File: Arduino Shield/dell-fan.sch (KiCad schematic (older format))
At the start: 49 parts, among them J1 Power, P1 Digital, P10 CONN_01X01, P11 CONN_01X01, P13 CONN_01X01, P2 Power, P3 Analog, P4 Analog, P5 PWM, P6 PWM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

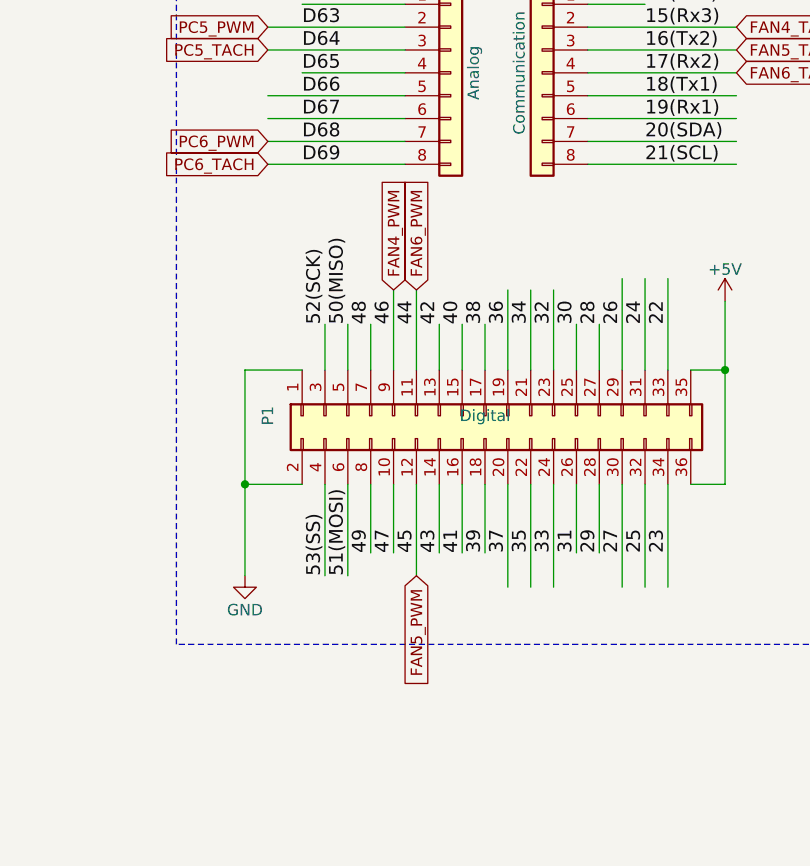
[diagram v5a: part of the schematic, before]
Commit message: redesign for rev 2.01.  Swapped PC and FAN location, and swapped FAN4_PWM and FAN5_PWM pins for simplicity
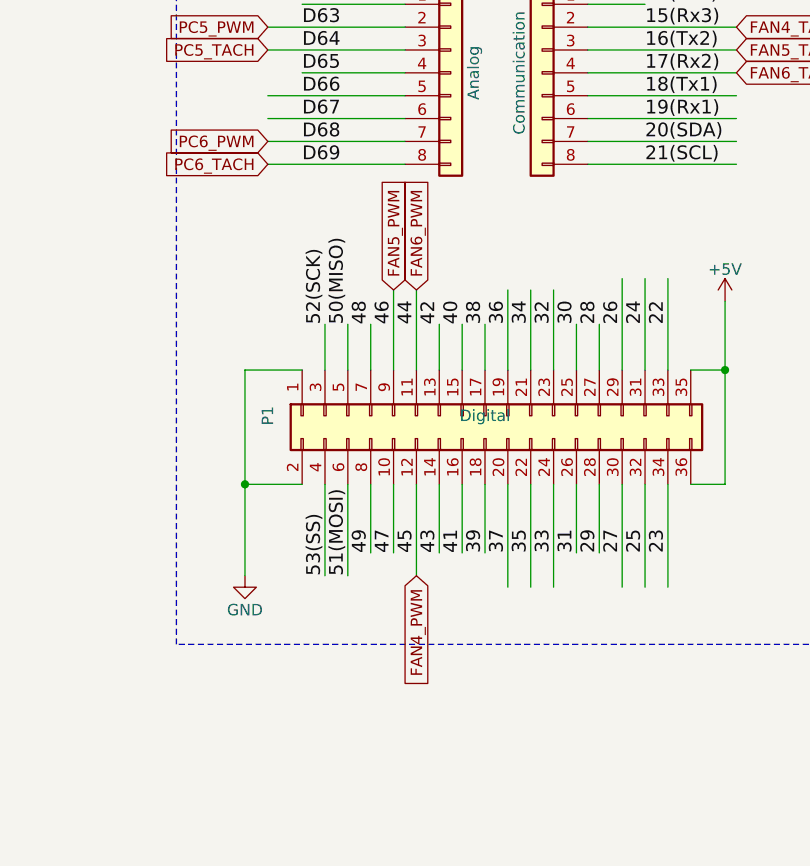
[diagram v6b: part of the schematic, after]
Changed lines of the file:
@@
 Text GLabel 10750 2400 2    50   Input ~ 0
 FAN3_PWM
+Text GLabel 9400 5750 3    50   Input ~ 0
+FAN4_PWM
 Text GLabel 9300 4500 1    50   Input ~ 0
-FAN4_PWM
-Text GLabel 9400 5750 3    50   Input ~ 0
 FAN5_PWM
 $Comp
